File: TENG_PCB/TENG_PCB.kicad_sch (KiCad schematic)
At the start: 22 parts, among them J1 1729128, J2 1729128, Q1 ZVN3310F, Q2 ZVP3310F, Q5 ZVN3310F, SW1 SW_DIP_x01

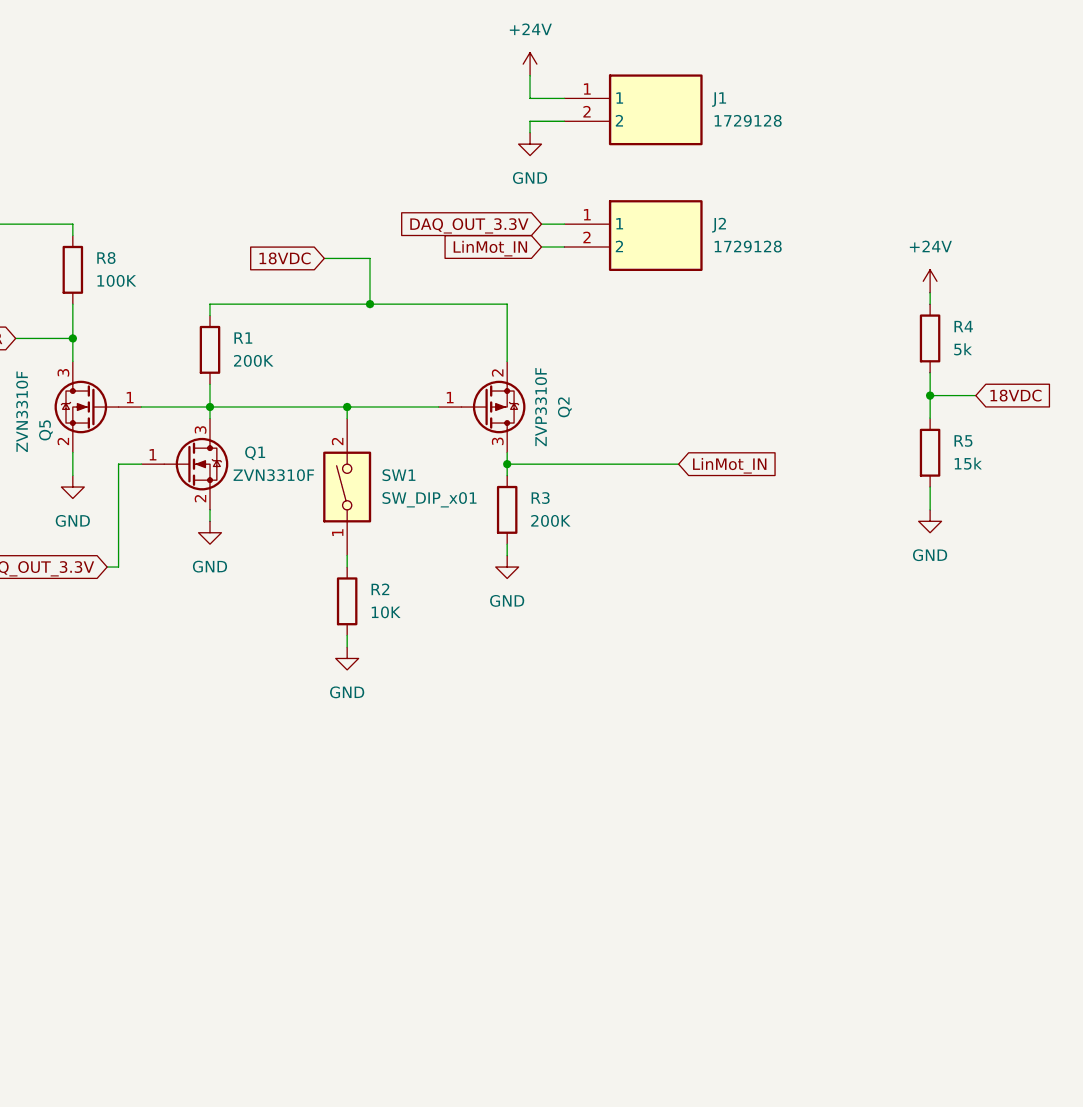
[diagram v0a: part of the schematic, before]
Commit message: Update TENG trigger PCB
Add trigger input ideas.
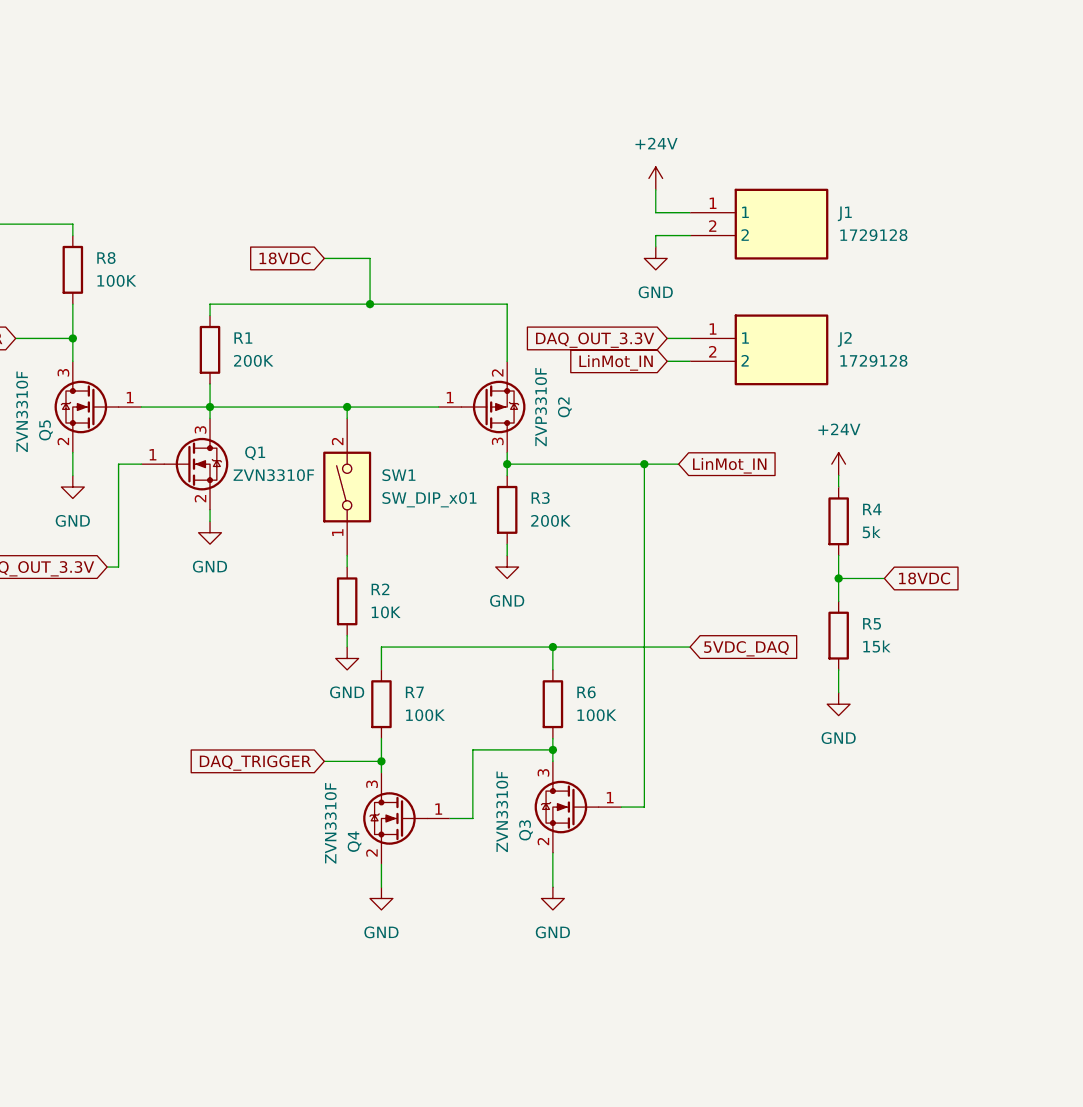
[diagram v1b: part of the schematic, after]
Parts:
- added Q3, Q4: ZVN3310F, Package_TO_SOT_SMD:SOT-23, symbol Transistor_FET:ZVN3310F
- added R6, R7: 100K, Resistor_SMD:R_0805_2012Metric, symbol Device:R
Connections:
- net 5VDC_DAQ: now also R6.1, R7.1
- net DAQ_TRIGGER: now also Q4.3 (D), R7.2
- net GND: now also Q3.2 (S), Q4.2 (S)
- net LinMot_IN: now also Q3.1 (G)
- new net: Q3.3 (D), Q4.1 (G), R6.2
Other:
- moved on the sheet: J1, J2, R4, R5
